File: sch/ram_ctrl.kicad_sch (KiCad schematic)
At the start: 11 parts

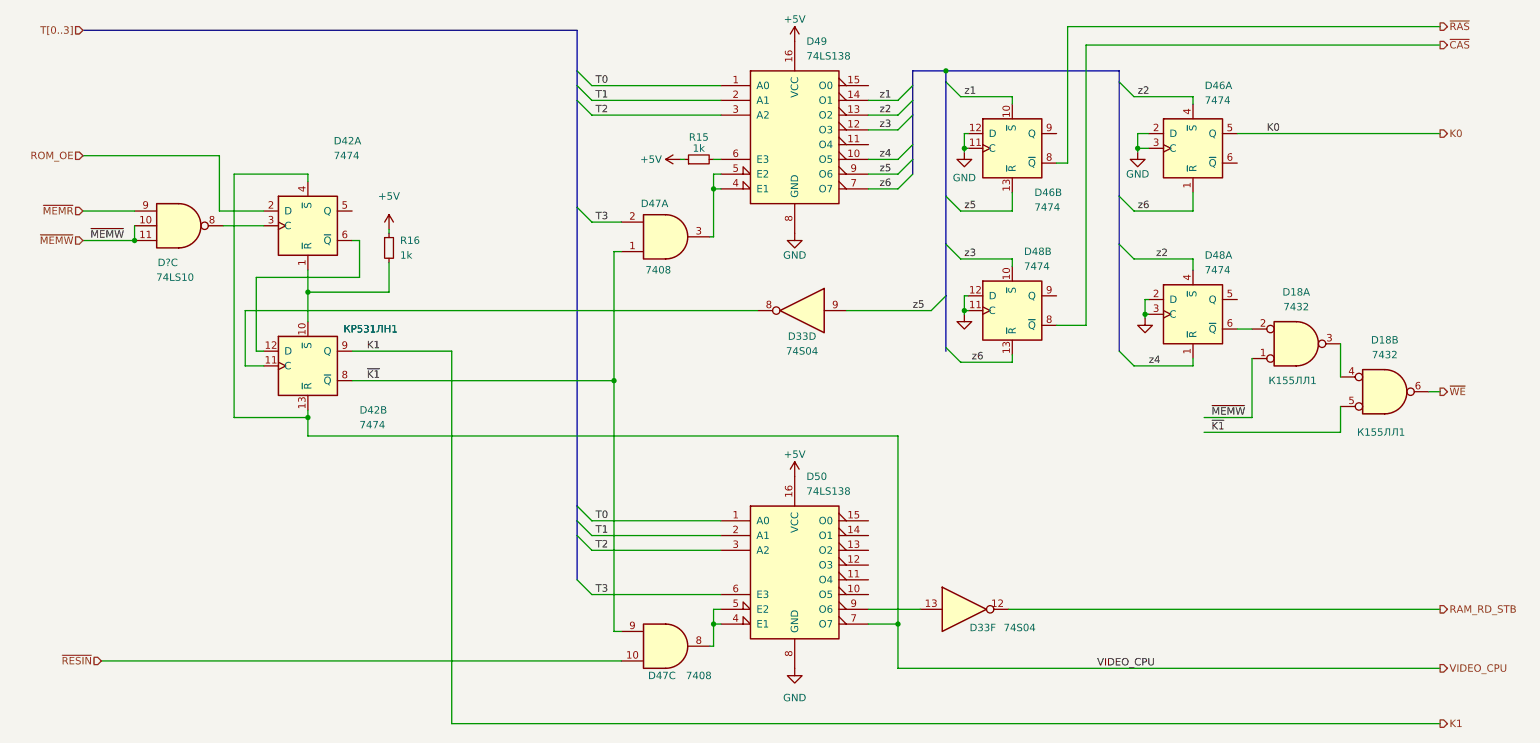
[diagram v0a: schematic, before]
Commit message: Sch: visual corrections
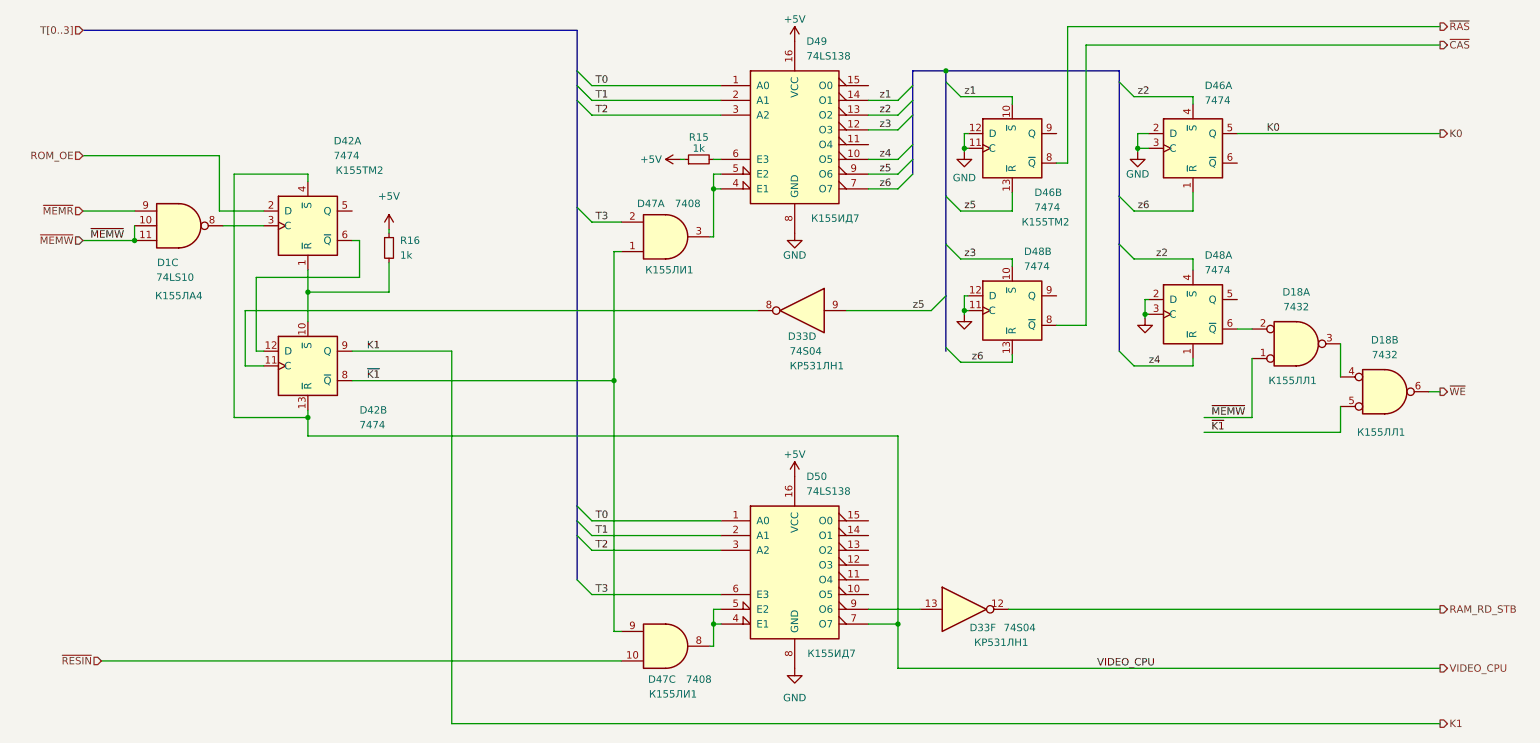
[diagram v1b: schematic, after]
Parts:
- D1: renamed from D?; CCCP (none) -> К155ЛА4
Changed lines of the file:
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@@
   (symbol (lib_id "74xx:74LS10") (at 47.625 60.96 0) (unit 3)
     (in_bom yes) (on_board yes)
-    (property "Reference" "D?" (id 0) (at 45.72 67.31 0))
+    (property "Reference" "D1" (id 0) (at 45.72 67.31 0))
     (property "Value" "74LS10" (id 1) (at 46.99 69.85 0))
     (property "Footprint" "" (id 2) (at 47.625 60.96 0)
@@
       (effects (font (size 1.27 1.27)) hide)
     )
+    (property "CCCP" "К155ЛА4" (id 4) (at 47.625 73.025 0))
     (pin "1")
     (pin "12")
@@
     (in_bom yes) (on_board yes)
     (property "Reference" "D33" (id 0) (at 154.94 80.01 0))
-    (property "Value" "74S04" (id 1) (at 154.94 82.55 0))
+    (property "Value" "74S04" (id 1) (at 155.575 82.55 0))
     (property "Footprint" "" (id 2) (at 154.94 75.565 0)
       (effects (font (size 1.27 1.27)) hide)
@@
       (effects (font (size 1.27 1.27)) hide)
     )
-    (property "CCCP" "КР531ЛН1" (id 4) (at 80.645 78.74 0))
+    (property "CCCP" "КР531ЛН1" (id 4) (at 157.48 85.09 0))
     (pin "1")
     (pin "2")
@@
   (symbol (lib_id "74xx:74LS08") (at 131.445 133.35 0) (unit 3)
     (in_bom yes) (on_board yes)
-    (property "Reference" "D47" (id 0) (at 130.81 138.43 0))
-    (property "Value" "7408" (id 1) (at 137.16 138.43 0))
+    (property "Reference" "D47" (id 0) (at 130.81 139.065 0))
+    (property "Value" "7408" (id 1) (at 137.16 139.065 0))
     (property "Footprint" "" (id 2) (at 131.445 133.35 0)
       (effects (font (size 1.27 1.27)) hide)
@@
       (effects (font (size 1.27 1.27)) hide)
     )
-    (property "CCCP" "К155ЛИ1" (id 4) (at 131.445 133.35 0)
-      (effects (font (size 1.27 1.27)) hide)
-    )
+    (property "CCCP" "К155ЛИ1" (id 4) (at 132.715 141.605 0))
     (pin "1")
     (pin "2")
@@
       (effects (font (size 1.27 1.27)) hide)
     )
-    (property "CCCP" "КР531ЛН1" (id 4) (at 80.645 78.74 0))
+    (property "CCCP" "КР531ЛН1" (id 4) (at 189.23 132.715 0))
     (pin "1")
     (pin "2")
@@
   (symbol (lib_id "74xx:74LS08") (at 131.445 62.865 0) (mirror x) (unit 1)
     (in_bom yes) (on_board yes)
-    (property "Reference" "D47" (id 0) (at 129.54 57.15 0))
-    (property "Value" "7408" (id 1) (at 130.175 68.58 0))
+    (property "Reference" "D47" (id 0) (at 128.905 57.15 0))
+    (property "Value" "7408" (id 1) (at 135.255 57.15 0))
     (property "Footprint" "" (id 2) (at 131.445 62.865 0)
       (effects (font (size 1.27 1.27)) hide)
@@
       (effects (font (size 1.27 1.27)) hide)
     )
-    (property "CCCP" "К155ЛИ1" (id 4) (at 131.445 62.865 0)
-      (effects (font (size 1.27 1.27)) hide)
-    )
+    (property "CCCP" "К155ЛИ1" (id 4) (at 132.08 68.58 0))
     (pin "1")
     (pin "2")
@@
       (effects (font (size 1.27 1.27)) hide)
     )
-    (property "CCCP" "К155ТМ2" (id 4) (at 191.135 47.625 0)
-      (effects (font (size 1.27 1.27)) hide)
-    )
+    (property "CCCP" "К155ТМ2" (id 4) (at 196.85 60.325 0))
     (pin "1")
     (pin "2")
@@
       (effects (font (size 1.27 1.27)) hide)
     )
-    (property "CCCP" "К155ТМ2" (id 4) (at 69.85 60.96 0)
-      (effects (font (size 1.27 1.27)) hide)
-    )
+    (property "CCCP" "К155ТМ2" (id 4) (at 78.74 51.435 0))
     (pin "1")
     (pin "2")
@@
   )
   (symbol (lib_id "74xx:74LS138") (at 153.67 119.38 0) (unit 1)
-    (in_bom yes) (on_board yes) (fields_autoplaced)
+    (in_bom yes) (on_board yes)
     (property "Reference" "D50" (id 0) (at 155.6894 104.14 0)
       (effects (font (size 1.27 1.27)) (justify left))
@@
       (effects (font (size 1.27 1.27)) hide)
     )
-    (property "CCCP" "К155ИД7" (id 4) (at 153.67 119.38 0)
-      (effects (font (size 1.27 1.27)) hide)
-    )
+    (property "CCCP" "К155ИД7" (id 4) (at 160.02 134.62 0))
     (pin "1")
     (pin "10")
@@
   )
   (symbol (lib_id "74xx:74LS138") (at 153.67 44.45 0) (unit 1)
-    (in_bom yes) (on_board yes) (fields_autoplaced)
+    (in_bom yes) (on_board yes)
     (property "Reference" "D49" (id 0) (at 155.6894 29.21 0)
       (effects (font (size 1.27 1.27)) (justify left))
@@
       (effects (font (size 1.27 1.27)) hide)
     )
-    (property "CCCP" "К155ИД7" (id 4) (at 153.67 44.45 0)
-      (effects (font (size 1.27 1.27)) hide)
-    )
-    (pin "1")
-    (pin "10")
+    (property "CCCP" "К155ИД7" (id 4) (at 160.655 59.69 0))
+    (pin "1")
+    (pin "10")
